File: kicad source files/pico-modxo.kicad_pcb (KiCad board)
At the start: 2 copper layers, 45 x 57 mm, 14 parts, among them J1 XBOX_LPC, U1 Pico

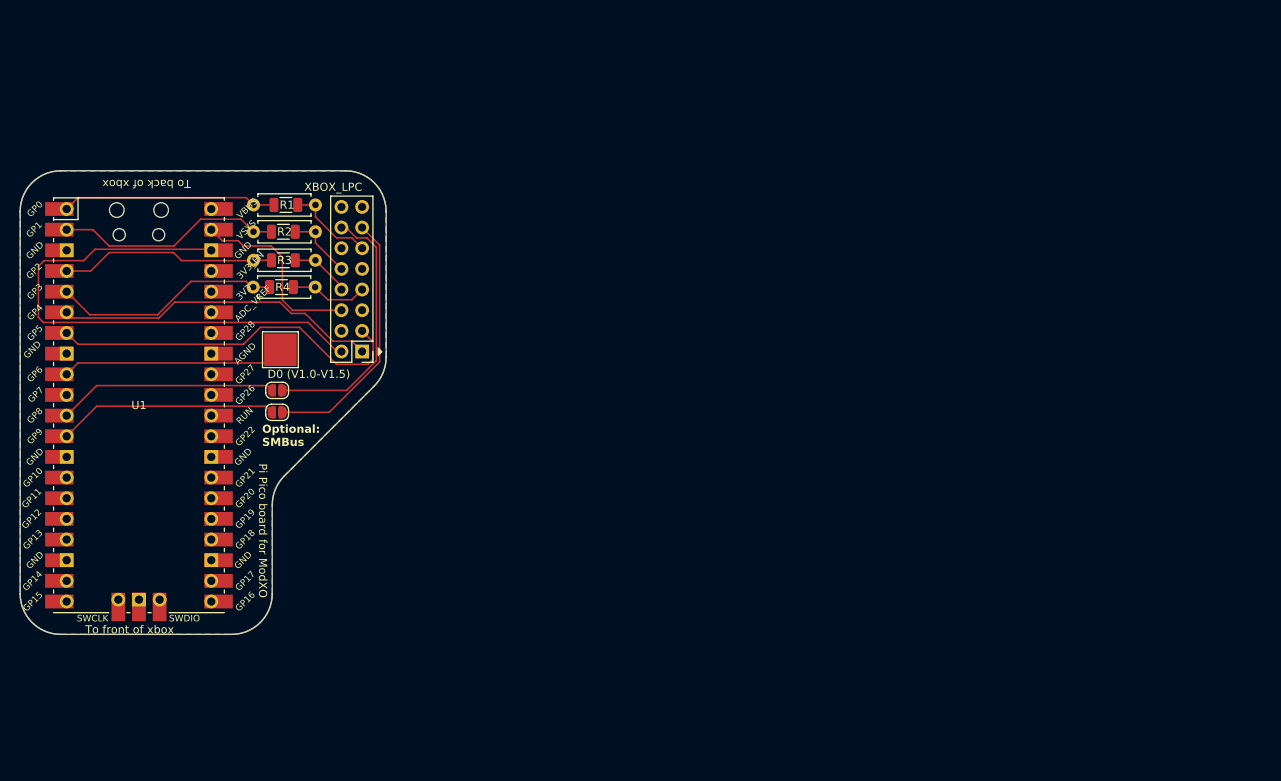
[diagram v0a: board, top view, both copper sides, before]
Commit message: V2 Design
V2 Design based on EqUiNoX schematic 1.0 2024-07-29
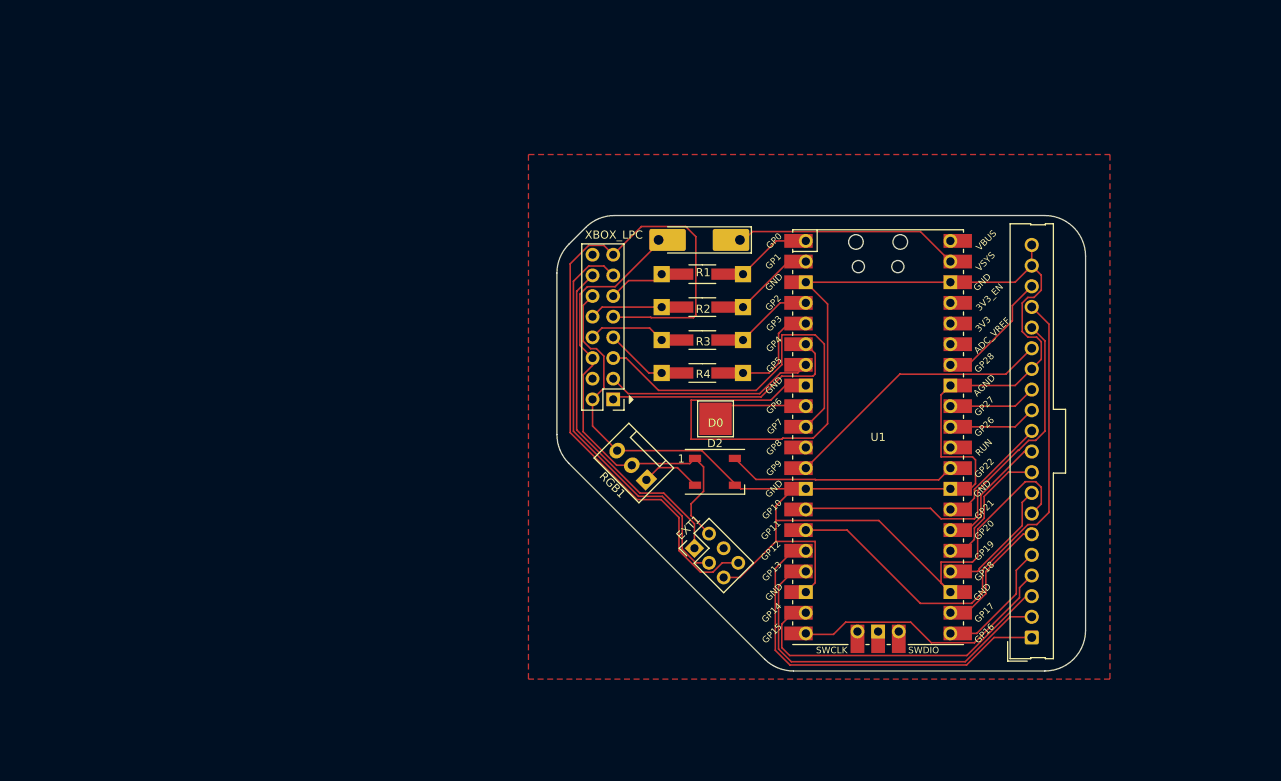
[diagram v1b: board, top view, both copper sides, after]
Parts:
- removed G***: LOGO, XBOX_LPC:modxo-logo
- removed JP1, JP2: SolderJumper_2_Open, Jumper:SolderJumper-2_P1.3mm_Open_RoundedPad1.0x1.5mm
- removed REF** (x4): R_1206_3216Metric, Resistor_SMD:R_1206_3216Metric
- added D1: RB551VM-30TE-17, Diode_SMD:D_MELF-RM10_Universal_Handsoldering, F.Cu at (128.5, 39.5)
- added D2: WS2812B, LED_SMD:LED_WS2812B_PLCC4_5.0x5.0mm_P3.2mm, F.Cu at (130.4, 68.0)
- added EXT1: Conn_02x03_Odd_Even, Connector_PinHeader_2.54mm:PinHeader_2x03_P2.54mm_Vertical, F.Cu at (127.9, 77.4)
- added J2: H2, Connector_Molex:Molex_SL_171971-0020_1x20_P2.54mm_Vertical, F.Cu at (169.4, 88.4)
- added RGB1: RGB1, Connector:FanPinHeader_1x03_P2.54mm_Vertical, F.Cu at (122.0, 69.0)
- J1: footprint XBOX_LPC:XBOX_LPC -> xbox_lpc:xbox_lpc
- R1, R2, R3, R4: footprint Resistor_THT:R_Axial_DIN0207_L6.3mm_D2.5mm_P7.62mm_Horizontal -> Resistors_Universal:Resistor_SMD+THTuniversal_1206_RM10_HandSoldering
- moved U1 91.0 mm to (150.5, 63.8)
- moved D0 54.2 mm to (130.5, 61.5)
- moved R4 48.8 mm to (128.9, 55.9), turned to 0 degrees
- moved R3 48.6 mm to (128.9, 51.8), turned to 0 degrees
- moved R2 48.5 mm to (128.9, 47.8), turned to 0 degrees
- moved R1 48.3 mm to (128.9, 43.7), turned to 0 degrees
- moved J1 31.4 mm to (117.9, 59.1)
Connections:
- net Net-(J1-LAD0) renamed LAD0
- net Net-(J1-LAD1) renamed LAD1
- net Net-(J1-LAD2) renamed LAD2
- net Net-(J1-LAD3) renamed LAD3
- net Net-(J1-LCLK) renamed LCLK
- net Net-(J1-LFRAME#) renamed LFRAME
- J1 pad 12: unconnected-(J1-GND-Pad12) -> GND
- J1 pad 13: Net-(J1-SCL) -> LSCL
- J1 pad 14: Net-(J1-SDA) -> LSDA
- J1 pad 15: unconnected-(J1-3.3V-Pad15) -> +3.3V
- J1 pad 5: unconnected-(J1-LRESET#-Pad5) -> LRESET
- J1 pad 6: +5V -> LPC_5V
- J1 pad 9: unconnected-(J1-3.3V-Pad9) -> +3.3V
- U1 pad 10: unconnected-(U1-GPIO7-Pad10) -> LRESET
- U1 pad 11: Net-(JP1-B) -> unconnected-(U1-GPIO8-Pad11)
- U1 pad 12: Net-(JP2-B) -> GPIO9
- U1 pad 14: unconnected-(U1-GPIO10-Pad14)_1 -> GPIO10
- U1 pad 15: unconnected-(U1-GPIO11-Pad15)_1 -> GPIO11
- U1 pad 16: unconnected-(U1-GPIO12-Pad16) -> SD_SPI1_MISO
- U1 pad 17: unconnected-(U1-GPIO13-Pad17) -> SD_SPI1_CS
- U1 pad 19: unconnected-(U1-GPIO14-Pad19)_1 -> SD_SPI1_SCK
- U1 pad 20: unconnected-(U1-GPIO15-Pad20)_1 -> SD_SPI1_MOSI
- U1 pad 21: unconnected-(U1-GPIO16-Pad21) -> UART_TX
- U1 pad 22: unconnected-(U1-GPIO17-Pad22) -> UART_RX
- U1 pad 24: unconnected-(U1-GPIO18-Pad24) -> DISPLAY_I2C1_SDA
- U1 pad 25: unconnected-(U1-GPIO19-Pad25) -> DISPLAY_I2C1_SCL
- U1 pad 26: unconnected-(U1-GPIO20-Pad26) -> EXT_I2C0_SDA
- U1 pad 27: unconnected-(U1-GPIO21-Pad27) -> EXT_I2C0_SCL
- U1 pad 29: unconnected-(U1-GPIO22-Pad29) -> RGBDI
- U1 pad 31: unconnected-(U1-GPIO26_ADC0-Pad31) -> DISPLAY_BRIGHTNESS
- U1 pad 32: unconnected-(U1-GPIO27_ADC1-Pad32) -> DISPLAY_CONTRAST
- U1 pad 34: unconnected-(U1-GPIO28_ADC2-Pad34) -> GPIO28
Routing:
- net GND: track 67.4 -> 280.5 mm
- net +3.3V: track 0.00 -> 90.2 mm
- net GPIO11: track 0.00 -> 66.0 mm
- net LPC_5V: track 0.00 -> 57.7 mm
- net LSCL: track 0.00 -> 50.3 mm
- net GPIO10: track 0.00 -> 49.7 mm
- net SD_SPI1_MISO: track 0.00 -> 48.4 mm
- net SD_SPI1_CS: track 0.00 -> 45.9 mm
- net LRESET: track 0.00 -> 44.2 mm
- net LSDA: track 0.00 -> 42.1 mm
- net SD_SPI1_SCK: track 0.00 -> 40.6 mm
- net GPIO9: track 0.00 -> 33.9 mm
- net SD_SPI1_MOSI: track 0.00 -> 33.6 mm
- net Net-(J1-SDA): track 32.3 -> 0.00 mm
- net Net-(J1-SCL): track 31.9 -> 0.00 mm
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- removed copper zone on B.Cu, net GND
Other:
- board size 45 x 57 mm -> 65 x 56 mm
- board text removed: "First true open-source modchip for Original XBOX. Thanks to ShalX"
- board text removed: "GND"
- board text removed: "Optional: SMBus"
- board text removed: "Pi Pico board for ModXO"
- board text removed: "Software: https://github.com/shalxmva/modxo Info: https://consolemods.org/wiki/Xbox:ModXo"
- board text removed: "To back of xbox"
- board text removed: "To front of xbox"

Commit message: Updated board to V2
See old 'V1' branch for original.
This V2 branch has suppport for LED / GPIO etc.
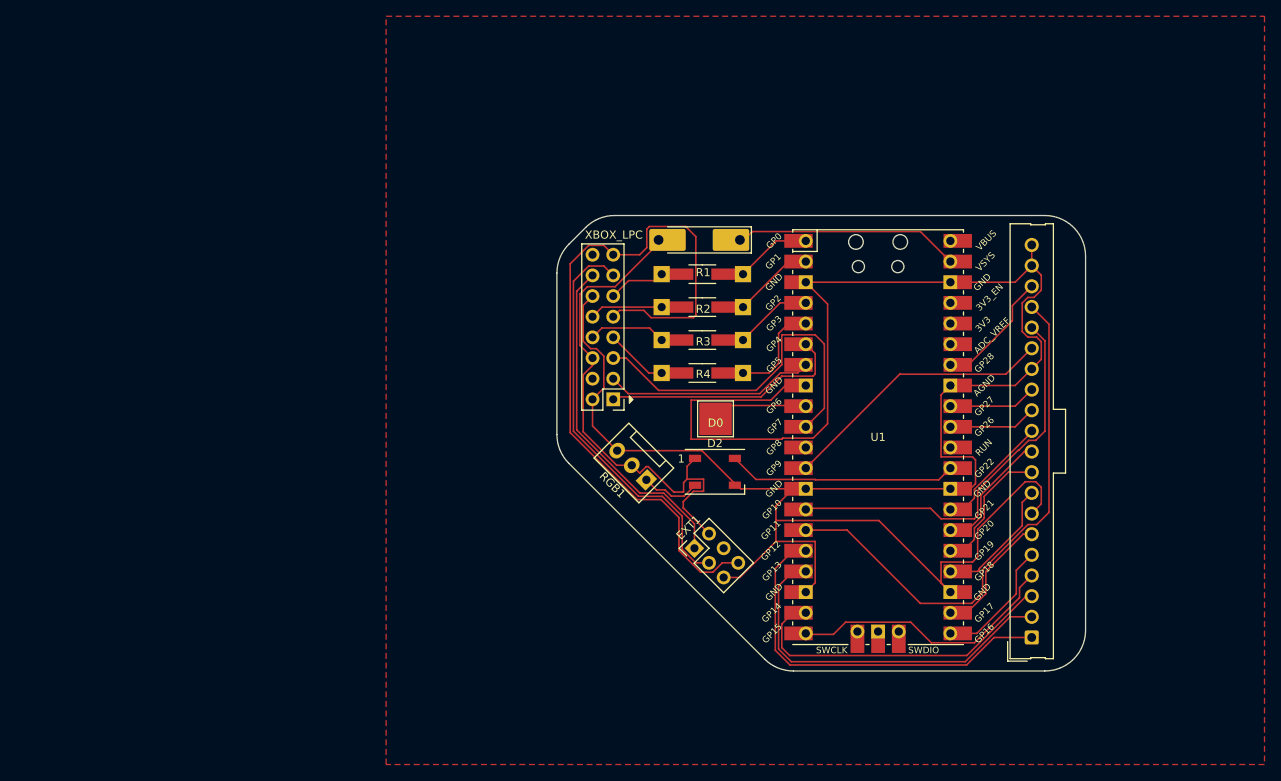
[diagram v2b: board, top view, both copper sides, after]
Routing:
- net LPC_5V: track 57.7 -> 63.3 mm
- net +3.3V: track 90.2 -> 92.2 mm
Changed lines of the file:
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@@
 		(layer "Edge.Cuts")
+	)
+	(dimension
+		(type aligned)
+		(layer "Dwgs.User")
+		(pts
+			(xy 169 92.5) (xy 169 36.5)
+		)
+		(height 17)
+		(gr_text "56,0000 mm"
+			(at 184.85 64.5 90)
+			(layer "Dwgs.User")
+			(effects
+				(font
+					(size 1 1)
+					(thickness 0.15)
+				)
+			)
+		)
+		(format
+			(prefix "")
+			(suffix "")
+			(units 3)
+			(units_format 1)
+			(precision 4)
+		)
+		(style
+			(thickness 0.1)
+			(arrow_length 1.27)
+			(text_position_mode 0)
+			(extension_height 0.58642)
+			(extension_offset 0.5) keep_text_aligned)
+	)
+	(dimension
+		(type aligned)
+		(layer "Dwgs.User")
+		(pts
+			(xy 111 53.5) (xy 176 53.5)
+		)
+		(height -26.5)
+		(gr_text "65,0000 mm"
+			(at 143.5 25.85 0)
+			(layer "Dwgs.User")
+			(effects
+				(font
+					(size 1 1)
+					(thickness 0.15)
+				)
+			)
+		)
+		(format
+			(prefix "")
+			(suffix "")
+			(units 3)
+			(units_format 1)
+			(precision 4)
+		)
+		(style
+			(thickness 0.1)
+			(arrow_length 1.27)
+			(text_position_mode 0)
+			(extension_height 0.58642)
+			(extension_offset 0.5) keep_text_aligned)
 	)
 	(segment
@@
 	)
 	(segment
-		(start 127.34 67)
-		(end 127.98 66.36)
+		(start 121.17622 68.17622)
+		(end 121.981801 67.370639)
 		(width 0.2)
 		(layer "F.Cu")
@@
 	(segment
 		(start 129.703949 75.611847)
-		(end 127.5 73.407898)
+		(end 126.592102 72.5)
 		(width 0.2)
 		(layer "F.Cu")
@@
 	)
 	(segment
+		(start 127 67.34)
+		(end 127.98 66.36)
+		(width 0.2)
+		(layer "F.Cu")
+		(net 2)
+	)
+	(segment
+		(start 122.230331 67.370639)
+		(end 125.359692 70.5)
+		(width 0.2)
+		(layer "F.Cu")
+		(net 2)
+	)
+	(segment
+		(start 125.359692 70.5)
+		(end 126.574314 70.5)
+		(width 0.2)
+		(layer "F.Cu")
+		(net 2)
+	)
+	(segment
 		(start 118.344259 67.203949)
 		(end 120.203949 67.203949)
@@
 	)
 	(segment
+		(start 129.03 70.41)
+		(end 129.03 68.91)
+		(width 0.2)
+		(layer "F.Cu")
+		(net 2)
+	)
+	(segment
 		(start 114.75 45.25)
 		(end 113.83 46.17)
@@
 	)
 	(segment
-		(start 127.5 73.407898)
-		(end 127.5 71.94)
+		(start 126.592102 72.5)
+		(end 126.565686 72.5)
+		(width 0.2)
+		(layer "F.Cu")
+		(net 2)
+	)
+	(segment
+		(start 120.203949 67.203949)
+		(end 121.17622 68.17622)
+		(width 0.2)
+		(layer "F.Cu")
+		(net 2)
+	)
+	(segment
+		(start 126.532843 71.672843)
+		(end 127.795686 70.41)
+		(width 0.2)
+		(layer "F.Cu")
+		(net 2)
+	)
+	(segment
+		(start 121.981801 67.370639)
+		(end 122.230331 67.370639)
 		(width 0.2)
 		(layer "F.Cu")
@@
 	)
 	(segment
-		(start 120.907898 67)
-		(end 127.34 67)
+		(start 126.574314 69.335686)
+		(end 127 68.91)
+		(width 0.2)
+		(layer "F.Cu")
+		(net 2)
+	)
+	(segment
+		(start 126.565686 72.5)
+		(end 126.532843 72.467157)
+		(width 0.2)
+		(layer "F.Cu")
+		(net 2)
+	)
+	(segment
+		(start 127 68.91)
+		(end 127 67.34)
 		(width 0.2)
 		(layer "F.Cu")
@@
 	)
 	(segment
-		(start 127.5 71.94)
-		(end 129.03 70.41)
-		(width 0.2)
-		(layer "F.Cu")
-		(net 2)
-	)
-	(segment
-		(start 120.203949 67.203949)
-		(end 120.703949 67.203949)
-		(width 0.2)
-		(layer "F.Cu")
-		(net 2)
-	)
-	(segment
-		(start 129.03 70.41)
-		(end 129.03 67.41)
-		(width 0.2)
-		(layer "F.Cu")
-		(net 2)
-	)
-	(segment
 		(start 114.23 63.08969)
 		(end 118.344259 67.203949)
@@
 	)
 	(segment
+		(start 129.03 68.91)
+		(end 127 68.91)
+		(width 0.2)
+		(layer "F.Cu")
+		(net 2)
+	)
+	(segment
 		(start 113.83 52.47)
 		(end 115.38 54.02)
@@
 	)
 	(segment
-		(start 129.03 67.41)
-		(end 127.98 66.36)
-		(width 0.2)
-		(layer "F.Cu")
-		(net 2)
-	)
-	(segment
-		(start 120.703949 67.203949)
-		(end 120.907898 67)
+		(start 126.532843 72.467157)
+		(end 126.532843 71.672843)
+		(width 0.2)
+		(layer "F.Cu")
+		(net 2)
+	)
+	(segment
+		(start 127.795686 70.41)
+		(end 129.03 70.41)
+		(width 0.2)
+		(layer "F.Cu")
+		(net 2)
+	)
+	(segment
+		(start 126.574314 70.5)
+		(end 126.574314 69.335686)
 		(width 0.2)
 		(layer "F.Cu")
@@
 	)
 	(segment
-		(start 125.82 67.5)
+		(start 122 69)
+		(end 123.229361 70.229361)
+		(width 0.2)
+		(layer "F.Cu")
+		(net 4)
+	)
+	(segment
+		(start 124.295047 70.229361)
+		(end 125.065686 71)
+		(width 0.2)
+		(layer "F.Cu")
+		(net 4)
+	)
+	(segment
+		(start 126.64 71)
 		(end 127.98 69.66)
 		(width 0.2)
@@
 	)
 	(segment
-		(start 123.5 67.5)
-		(end 125.82 67.5)
+		(start 125.065686 71)
+		(end 126.64 71)
 		(width 0.2)
 		(layer "F.Cu")
@@
 	)
 	(segment
-		(start 122 69)
-		(end 123.5 67.5)
+		(start 123.229361 70.229361)
+		(end 124.295047 70.229361)
 		(width 0.2)
 		(layer "F.Cu")
@@
 	)
 	(segment
-		(start 117.98 49)
-		(end 122.51976 49)
-		(width 0.2)
-		(layer "F.Cu")
-		(net 6)
-	)
-	(segment
 		(start 112.63 63.186748)
 		(end 120.872613 71.429361)
@@
 	)
 	(segment
-		(start 121.39 37.85)
-		(end 117.92 41.32)
-		(width 0.2)
-		(layer "F.Cu")
-		(net 6)
-	)
-	(segment
 		(start 114.903654 40.17)
 		(end 112.63 42.443654)
@@
 	)
 	(segment
+		(start 121.67976 48.16)
+		(end 122.57925 49.05949)
+		(width 0.2)
+		(layer "F.Cu")
+		(net 6)
+	)
+	(segment
+		(start 122.365256 37.85)
+		(end 122.05 38.165256)
+		(width 0.2)
+		(layer "F.Cu")
+		(net 6)
+	)
+	(segment
+		(start 122.05 38.165256)
+		(end 122.05 40.45)
+		(width 0.2)
+		(layer "F.Cu")
+		(net 6)
+	)
+	(segment
+		(start 128.07891 48.75977)
+		(end 128.07891 39.094166)
+		(width 0.2)
+		(layer "F.Cu")
+		(net 6)
+	)
+	(segment
+		(start 126.005816 73.637188)
+		(end 126.005816 77.697848)
+		(width 0.2)
+		(layer "F.Cu")
+		(net 6)
+	)
+	(segment
+		(start 126.834744 37.85)
+		(end 122.365256 37.85)
+		(width 0.2)
+		(layer "F.Cu")
+		(net 6)
+	)
+	(segment
+		(start 122.05 40.45)
+		(end 121.18 41.32)
+		(width 0.2)
+		(layer "F.Cu")
+		(net 6)
+	)
+	(segment
+		(start 128.661917 80.353949)
+		(end 130.180295 80.353949)
+		(width 0.2)
+		(layer "F.Cu")
+		(net 6)
+	)
+	(segment
+		(start 127.77919 49.05949)
+		(end 128.07891 48.75977)
+		(width 0.2)
+		(layer "F.Cu")
+		(net 6)
+	)
+	(segment
+		(start 128.07891 39.094166)
+		(end 126.834744 37.85)
+		(width 0.2)
+		(layer "F.Cu")
+		(net 6)
+	)
+	(segment
+		(start 117.92 48.94)
+		(end 118.7 48.16)
+		(width 0.2)
+		(layer "F.Cu")
+		(net 6)
+	)
+	(segment
+		(start 126.005816 77.697848)
+		(end 128.661917 80.353949)
+		(width 0.2)
+		(layer "F.Cu")
+		(net 6)
+	)
+	(segment
 		(start 122.57925 49.05949)
 		(end 127.77919 49.05949)
@@
 	)
 	(segment
-		(start 128.07891 48.75977)
-		(end 128.07891 39.094166)
-		(width 0.2)
-		(layer "F.Cu")
-		(net 6)
-	)
-	(segment
-		(start 126.005816 73.637188)
-		(end 126.005816 77.697848)
-		(width 0.2)
-		(layer "F.Cu")
-		(net 6)
-	)
-	(segment
-		(start 128.07891 39.094166)
-		(end 126.834744 37.85)
-		(width 0.2)
-		(layer "F.Cu")
-		(net 6)
-	)
-	(segment
-		(start 126.834744 37.85)
-		(end 121.39 37.85)
-		(width 0.2)
-		(layer "F.Cu")
-		(net 6)
-	)
-	(segment
-		(start 128.661917 80.353949)
-		(end 130.180295 80.353949)
-		(width 0.2)
-		(layer "F.Cu")
-		(net 6)
-	)
-	(segment
-		(start 126.005816 77.697848)
-		(end 128.661917 80.353949)
-		(width 0.2)
-		(layer "F.Cu")
-		(net 6)
-	)
-	(segment
-		(start 127.77919 49.05949)
-		(end 128.07891 48.75977)
-		(width 0.2)
-		(layer "F.Cu")
-		(net 6)
-	)
-	(segment
-		(start 117.92 48.94)
-		(end 117.98 49)
-		(width 0.2)
-		(layer "F.Cu")
-		(net 6)
-	)
-	(segment
 		(start 120.872613 71.429361)
 		(end 123.797989 71.429361)
@@
 	)
 	(segment
-		(start 122.51976 49)
-		(end 122.57925 49.05949)
+		(start 121.18 41.32)
+		(end 117.92 41.32)
+		(width 0.2)
+		(layer "F.Cu")
+		(net 6)
+	)
+	(segment
+		(start 118.7 48.16)
+		(end 121.67976 48.16)
 		(width 0.2)
 		(layer "F.Cu")
@@
 		(polygon
 			(pts
-				(xy 107.5 29) (xy 179 29) (xy 179 93.5) (xy 107.5 93.5)
+				(xy 90 12) (xy 198 12) (xy 198 104) (xy 90 104)
 			)
 		)

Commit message: Move GND add GP8
added Gp8 connected to 3.3v
moved GND to bottom.
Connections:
- U1 pad 11: unconnected-(U1-GPIO8-Pad11) -> +3.3V
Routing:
- net GND: track 280.5 -> 2.66 mm
- net +3.3V: track 92.2 -> 118.6 mm
- net DISPLAY_I2C1_SDA: track 15.8 -> 17.1 mm
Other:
- board text added: "GP12"

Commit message: RGB LED GND via
added via to Grad plain for RGB LED
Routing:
- net GND: track 2.66 -> 4.82 mm, vias 0 -> 1
- added copper zone on B.Cu, net GND
- removed copper zone on F.Cu, net GND
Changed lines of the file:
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@@
+	(segment
+		(start 132.88 69.66)
+		(end 134.91 69.66)
+		(width 0.2)
+		(layer "F.Cu")
+		(net 8)
+	)
+	(segment
+		(start 134.91 69.66)
+		(end 135 69.75)
+		(width 0.2)
+		(layer "F.Cu")
+		(net 8)
+	)
 	(segment
 		(start 132.88 69.66)
@@
 		(width 0.2)
 		(layer "F.Cu")
+		(net 8)
+	)
+	(via
+		(at 135 69.75)
+		(size 0.6)
+		(drill 0.3)
+		(layers "F.Cu" "B.Cu")
+		(free yes)
 		(net 8)
 	)
@@
 		(net 8)
 		(net_name "GND")
-		(layer "F.Cu")
+		(layer "B.Cu")
 		(hatch edge 0.5)
 		(connect_pads
@@
 		(polygon
 			(pts
-				(xy 90 12) (xy 198 12) (xy 198 104) (xy 90 104)
+				(xy 89.25 35.75) (xy 197.25 35.75) (xy 198 104) (xy 90 104)
 			)
 		)

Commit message: Pico ModXo V1.0
Release V1.0
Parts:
- added G***: LOGO, xbox_lpc:modxo-logo, F.Cu at (150.5, 77.9)
- added G***: LOGO, xbox_lpc:team-resurgent-logo, F.Cu at (149.8, 59.7)
- added G***: LOGO, xbox_lpc:team-resurgent-logo, B.Cu at (149.6, 59.7)
- added G***: LOGO, xbox_lpc:modxo-logo, B.Cu at (150.4, 77.6)
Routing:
- net LPC_5V: track 63.3 -> 56.9 mm
- net +3.3V: track 118.6 -> 117.1 mm
- net DISPLAY_I2C1_SDA: track 17.1 -> 16.2 mm
- net SD_SPI1_MOSI: track 33.6 -> 34.4 mm
- net SD_SPI1_SCK: track 40.6 -> 41.3 mm
- net GND: track 4.82 -> 4.20 mm
- added copper zone on F.Cu, net GND
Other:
- board text added: "${REVISION}"
- board text added: "To XBOX front"
- board text added: "consolemods.org/wiki/Xbox:ModXo"
- board text added: "github.com/Electrical5/Pico-ModXo"
- board text added: "github.com/Team-Resurgent/Modxo"
- board text removed: "GP12"
